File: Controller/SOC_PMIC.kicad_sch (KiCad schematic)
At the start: 30 parts, among them U24 TPS22965DSGR, U3 TPS6521907RHBR

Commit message: Fixed some minor issues, started some scheamtic clean up
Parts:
- removed TP5: TestPoint, TestPoint:TestPoint_Pad_2.0x2.0mm, symbol Connector:TestPoint
- added R221, R222: 0R, Resistor_SMD:R_0603_1608Metric, symbol Device:R
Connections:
- net +3V3: now also R221.2
- net GND: now also R222.1
- net PMIC_MODE_STBY: now also R221.1, R222.2

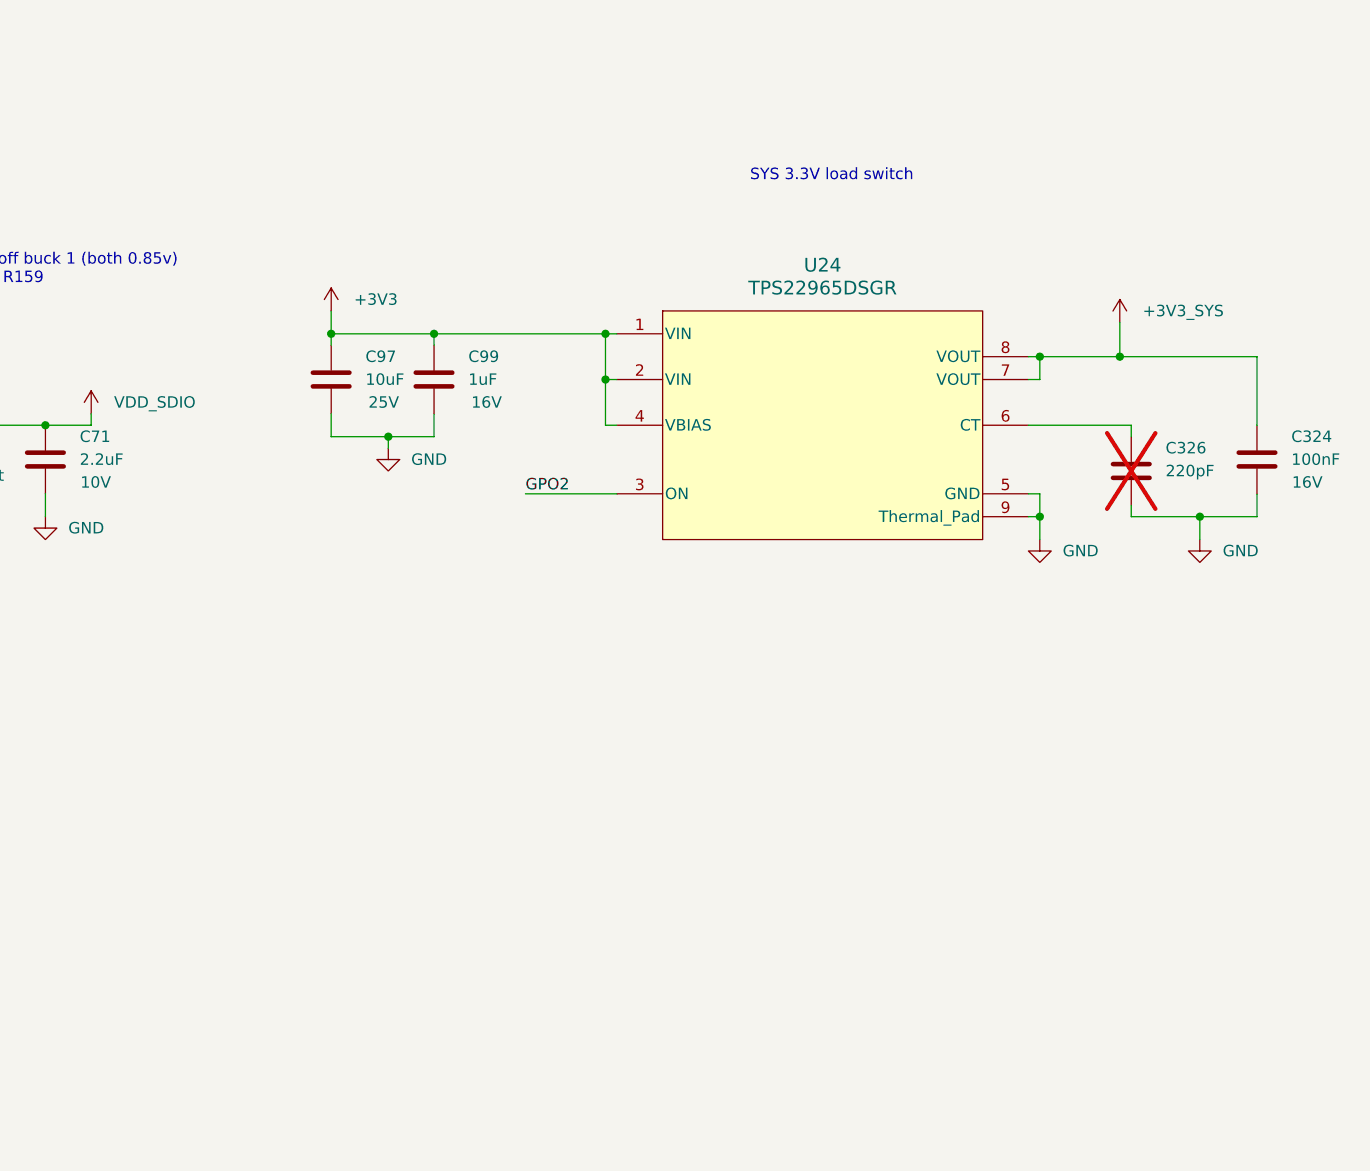
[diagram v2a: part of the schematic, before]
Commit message: DDR_CLK termination
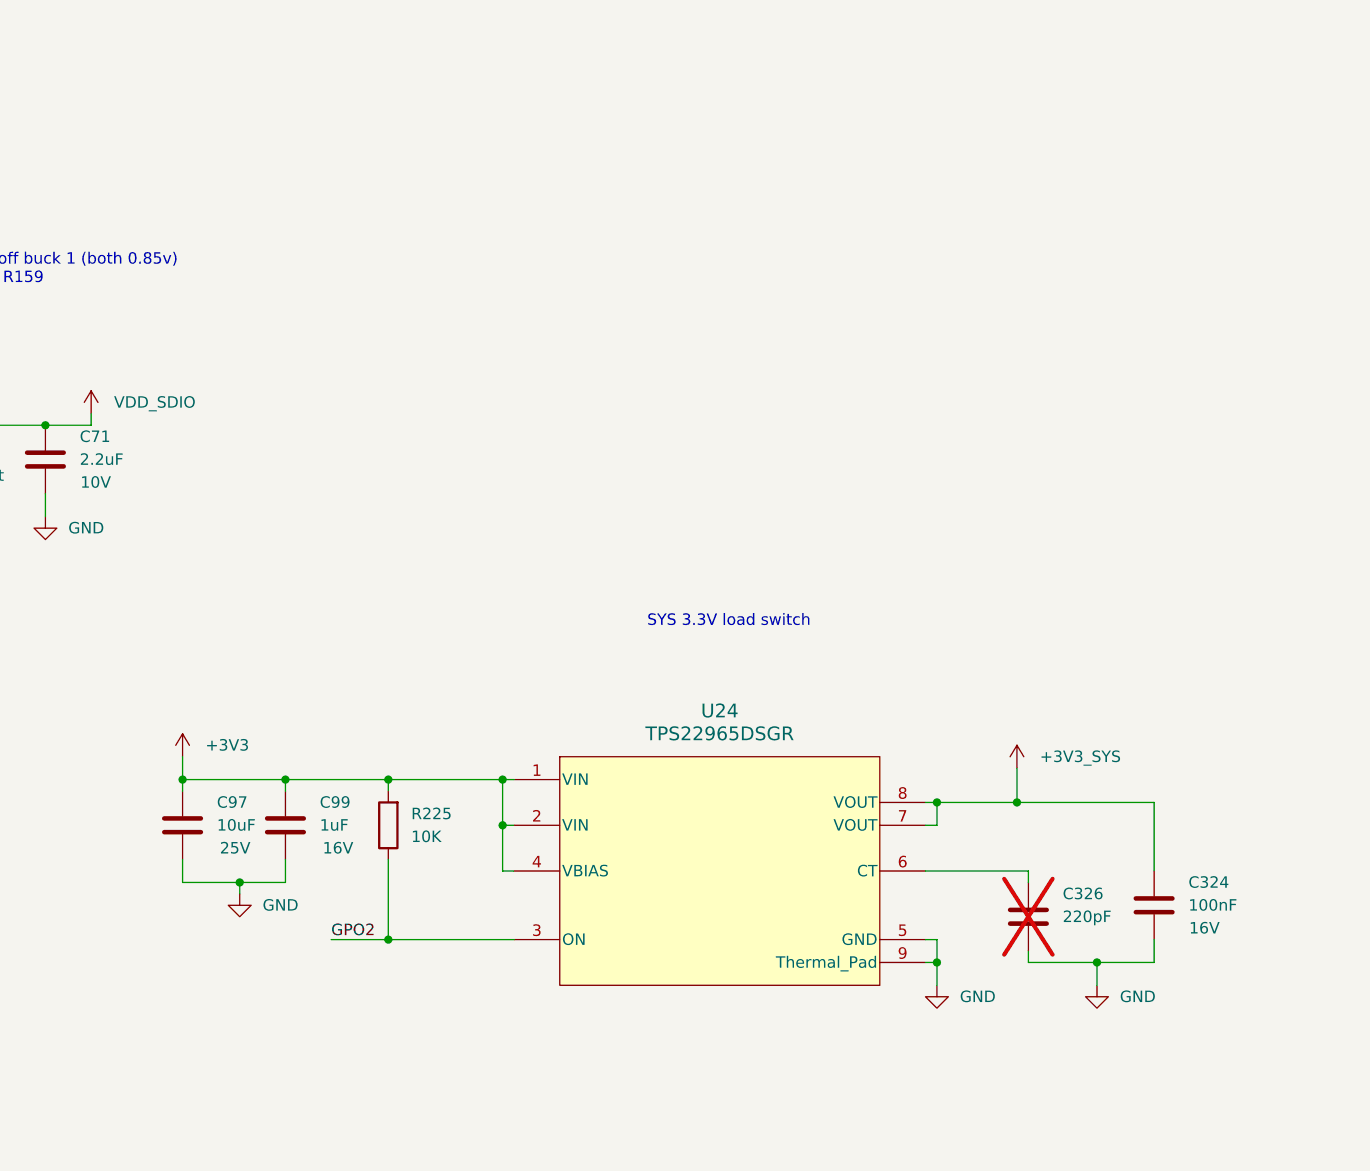
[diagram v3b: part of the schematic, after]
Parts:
- added R225: 10K, Resistor_SMD:R_0603_1608Metric, symbol Device:R
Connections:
- net +3V3: now also R225.2
- net GPO2: now also R225.1
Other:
- moved on the sheet: C324, C326, C97, C99, U24

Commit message: JTAG
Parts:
- U3: value TPS6521907RHBR -> TPS6521904RHBR; symbol TPS6521907RHBR:TPS6521907RHBR -> TPS6521907RHBR:TPS6521904RHBR
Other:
- note removed: "Part used actually TPS6521904 not 07. TODO: Update symbol part#"
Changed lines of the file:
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@@
 		)
 	)
-	(text "Part used actually TPS6521904 not 07. TODO: Update symbol part#"
-		(exclude_from_sim no)
-		(at 50.546 158.496 0)
-		(effects
-			(font
-				(size 1.27 1.27)
-			)
-		)
-	)
 	(junction
 		(at 295.91 151.13)
@@
 	)
 	(symbol
-		(lib_id "TPS6521907RHBR:TPS6521907RHBR")
+		(lib_id "TPS6521907RHBR:TPS6521904RHBR")
 		(at 107.95 66.04 0)
 		(unit 1)
@@
 			)
 		)
-		(property "Value" "TPS6521907RHBR"
+		(property "Value" "TPS6521904RHBR"
 			(at 140.97 58.42 0)
 			(show_name no)

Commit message: Testpoints + DDR velocity comp
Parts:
- added D48: LED, LED_SMD:LED_0603_1608Metric, symbol Device:LED
- added R235: 100R, Resistor_SMD:R_0603_1608Metric, symbol Device:R
- added TP10, TP11, TP12, TP13, TP14, TP15, TP16, TP21, TP22, TP32, TP33, TP9: TestPoint, TestPoint:TestPoint_Pad_D1.5mm, symbol Connector:TestPoint
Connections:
- net +3V3_SYS: now also R235.1
- net GND: now also D48.1 (K), TP15.1, TP16.1, TP33.1
- net GPO2: now also TP32.1
- net SOC_I2C0_SCL: now also TP21.1
- net SOC_I2C0_SDA: now also TP22.1
- net VCC_1V8: now also TP11.1
- net VCC_CORE: now also TP10.1
- net VDDA_1V8: now also TP13.1
- net VDD_1V2: now also TP9.1
- net VDD_2V5: now also TP14.1
- net VDD_SDIO: now also TP12.1
- new net: D48.2 (A), R235.2

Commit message: REV 1B
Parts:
- added R236: 0R, Resistor_SMD:R_0603_1608Metric, symbol Device:R
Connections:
- net PMIC_INT_N: now also R236.2; no longer U3.11 (INT_N)
- new net INT_N: R236.1, U3.11 (INT_N)
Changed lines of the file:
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@@
 	(wire
 		(pts
+			(xy 165.1 203.2) (xy 167.64 203.2)
+		)
+		(stroke
+			(width 0)
+			(type default)
+		)
+	)
+	(wire
+		(pts
 			(xy 273.05 133.35) (xy 284.48 133.35)
 		)
@@
 	(wire
 		(pts
-			(xy 179.07 132.08) (xy 173.99 132.08)
-		)
-		(stroke
-			(width 0)
-			(type default)
-		)
-	)
-	(wire
-		(pts
 			(xy 68.58 80.01) (xy 85.09 80.01)
 		)
@@
 	(wire
 		(pts
+			(xy 187.96 132.08) (xy 173.99 132.08)
+		)
+		(stroke
+			(width 0)
+			(type default)
+		)
+	)
+	(wire
+		(pts
 			(xy 107.95 78.74) (xy 104.14 78.74)
 		)
@@
 	(wire
 		(pts
+			(xy 149.86 203.2) (xy 157.48 203.2)
+		)
+		(stroke
+			(width 0)
+			(type default)
+		)
+	)
+	(wire
+		(pts
 			(xy 367.03 153.67) (xy 374.65 153.67)
 		)
@@
 		)
 	)
+	(label "INT_N"
+		(at 187.96 132.08 180)
+		(effects
+			(font
+				(size 1.27 1.27)
+			)
+			(justify right bottom)
+		)
+	)
 	(label "PMIC_SDA"
 		(at 22.86 181.61 0)
@@
 		)
 	)
+	(label "INT_N"
+		(at 149.86 203.2 0)
+		(effects
+			(font
+				(size 1.27 1.27)
+			)
+			(justify left bottom)
+		)
+	)
 	(label "GPO2"
 		(at 289.56 151.13 0)
@@
 	(global_label "PMIC_INT_N"
 		(shape input)
-		(at 179.07 132.08 0)
+		(at 167.64 203.2 0)
 		(fields_autoplaced yes)
 		(effects
@@
 		)
 		(property "Intersheetrefs" "${INTERSHEET_REFS}"
-			(at 192.82 132.08 0)
+			(at 181.39 203.2 0)
 			(hide yes)
 			(show_name no)
@@
 					(unit 1)
 				)
+			)
+		)
+	)
+	(symbol
+		(lib_id "Device:R")
+		(at 161.29 203.2 90)
+		(unit 1)
+		(body_style 1)
+		(exclude_from_sim no)
+		(in_bom yes)
+		(on_board yes)
+		(in_pos_files yes)
+		(dnp no)
+		(fields_autoplaced yes)
+		(property "Reference" "R236"
+			(at 161.29 196.85 90)
+			(show_name no)
+			(do_not_autoplace no)
+			(effects
+				(font
+					(size 1.27 1.27)
+				)
+			)
+		)
+		(property "Value" "0R"
+			(at 161.29 199.39 90)
+			(show_name no)
+			(do_not_autoplace no)
+			(effects
+				(font
+					(size 1.27 1.27)
+				)
+			)
+		)
+		(property "Footprint" "Resistor_SMD:R_0603_1608Metric"
+			(at 161.29 204.978 90)
+			(hide yes)
+			(show_name no)
+			(do_not_autoplace no)
+			(effects
+				(font
+					(size 1.27 1.27)
+				)
+			)
+		)
+		(property "Datasheet" ""
+			(at 161.29 203.2 0)
+			(hide yes)
+			(show_name no)
+			(do_not_autoplace no)
+			(effects
+				(font
+					(size 1.27 1.27)
+				)
+			)
+		)
+		(property "Description" "Resistor"
+			(at 161.29 203.2 0)
+			(hide yes)
+			(show_name no)
+			(do_not_autoplace no)
+			(effects
+				(font
+					(size 1.27 1.27)
+				)
+			)
+		)
+		(pin "2"
+		)
+		(pin "1"
+		)
+		(instances
+			(project "Controller"
+				(path "/2c9e7a41-63e4-4339-89dd-991e772f7a19/2b3b3ca2-9bcd-4196-8c9e-35d95e6d945f"
+					(reference "R236")
+					(unit 1)
+				)
